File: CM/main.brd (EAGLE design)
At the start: 100 x 80 mm, 16 parts, among them Q1 IRF520, Q2 IRF520, Q3 IRF520

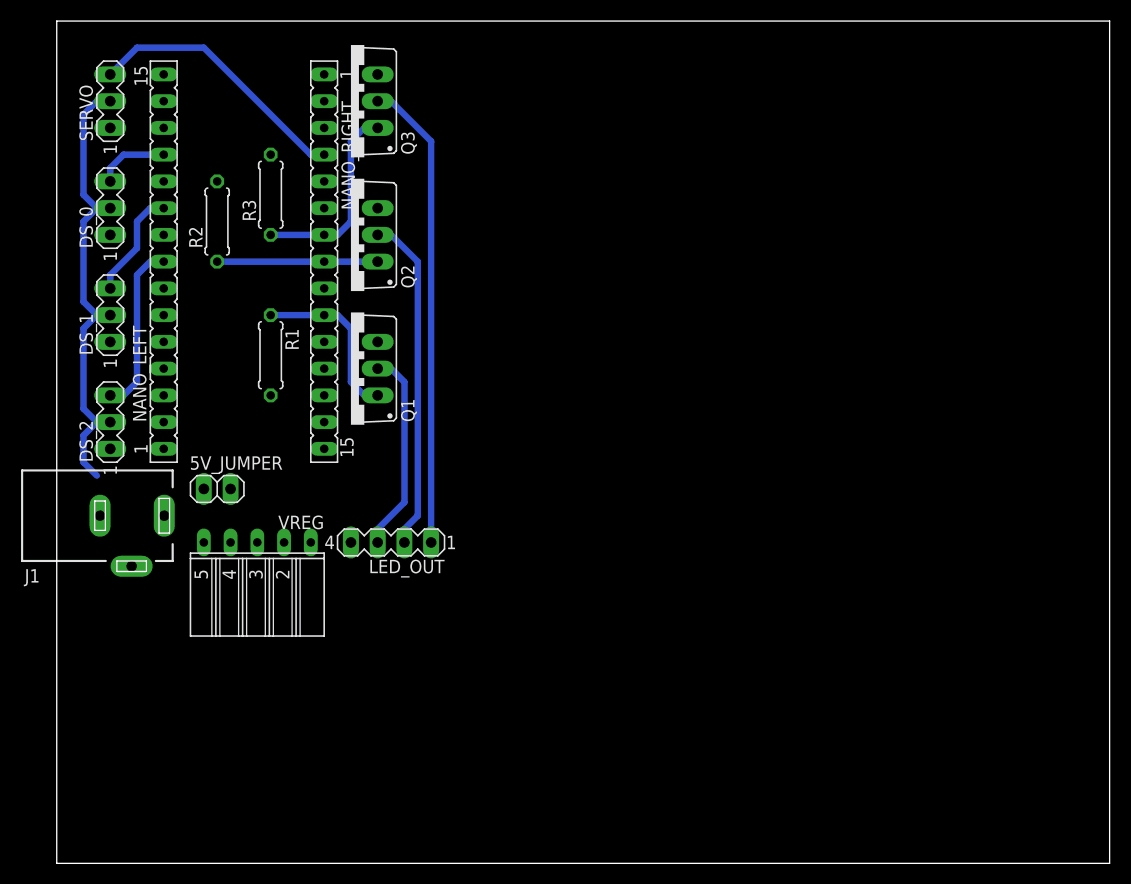
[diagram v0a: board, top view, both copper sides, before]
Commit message: Updated casemod circuit, added a few images
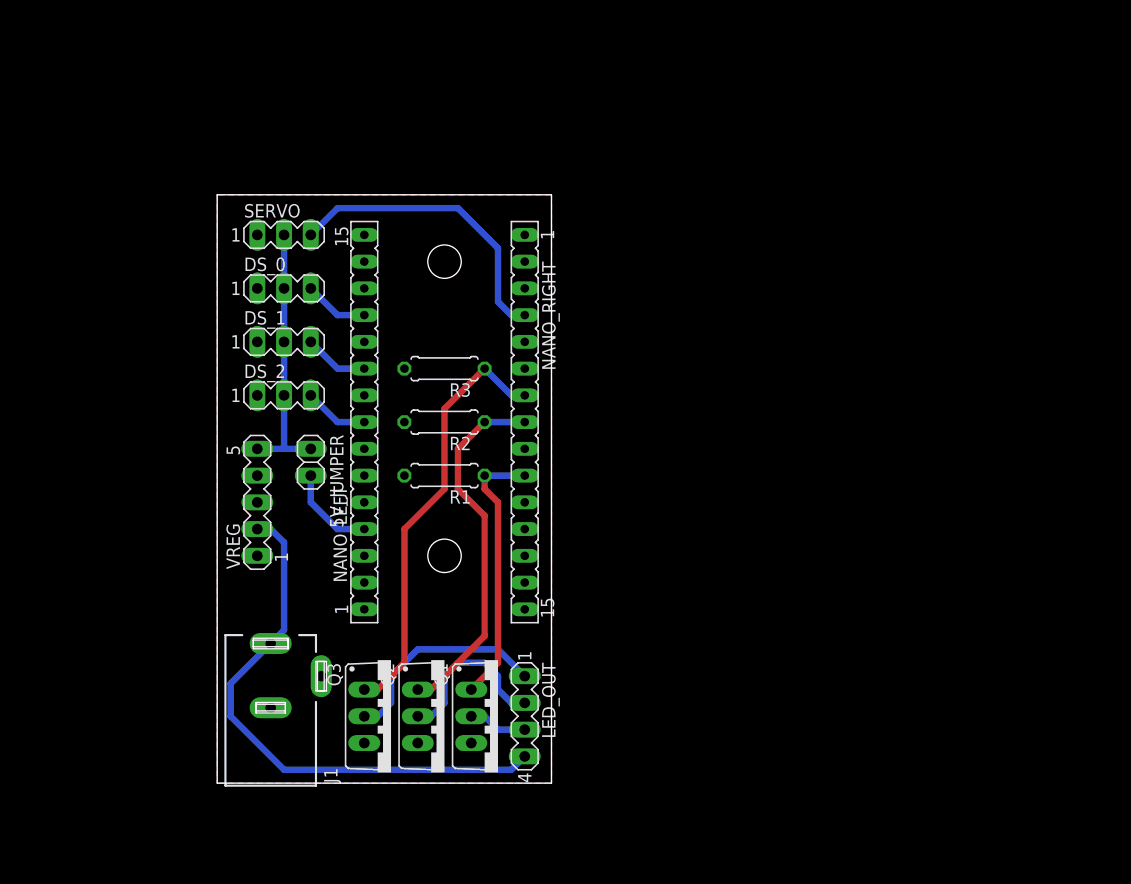
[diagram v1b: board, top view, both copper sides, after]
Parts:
- VREG: device con-lsta:FE05W -> con-lstb:MA05-1
- moved Q3 58.5 mm to (31.8, 14.0), turned to 270 degrees
- moved Q2 46.6 mm to (36.8, 14.0), turned to 270 degrees
- moved Q1 35.9 mm to (41.9, 14.0), turned to 270 degrees
- moved R2 28.8 mm to (36.8, 41.9), turned to 180 degrees
- moved NANO_RIGHT 24.4 mm to (44.5, 41.9)
- moved NANO_LEFT 24.4 mm to (29.2, 41.9)
- moved R3 23.3 mm to (36.8, 47.0), turned to 180 degrees
- moved LED_OUT 20.8 mm to (44.5, 14.0), turned to 270 degrees
- moved SERVO 20.8 mm to (21.6, 59.7), turned to 0 degrees
- moved J1 20.2 mm to (20.3, 17.8), turned to 0 degrees
- moved R1 20.1 mm to (36.8, 36.8), turned to 180 degrees
- moved DS_0 18.2 mm to (21.6, 54.6), turned to 0 degrees
- moved DS_2 16.7 mm to (21.6, 44.5), turned to 0 degrees
- moved DS_1 16.7 mm to (21.6, 49.5), turned to 0 degrees
- moved 5V_JUMPER 9.25 mm to (24.1, 38.1), turned to 270 degrees
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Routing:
- net 12V: track 0.00 -> 52.3 mm
- net B_OUT: track 44.8 -> 20.4 mm
- net B_CTL: track 18.8 -> 40.8 mm
- net 5V: track 44.8 -> 25.4 mm
- net R_CTL: track 15.2 -> 34.7 mm
- net R_OUT: track 32.1 -> 16.1 mm
- net G_OUT: track 19.4 -> 5.61 mm
- net A4: track 16.3 -> 6.13 mm
- net G_CTL: track 16.3 -> 25.7 mm
- net 5V_JMP: track 0.00 -> 8.67 mm
- net A2: track 10.5 -> 6.13 mm
- net S_CTL: track 25.6 -> 28.6 mm
- net A0: track 6.88 -> 6.13 mm
- added copper zone on layer 1, net GND
- added copper zone on layer 16, net GND
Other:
- board size 100 x 80 mm -> 31.8 x 55.9 mm
